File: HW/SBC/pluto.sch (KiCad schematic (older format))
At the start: 0 parts

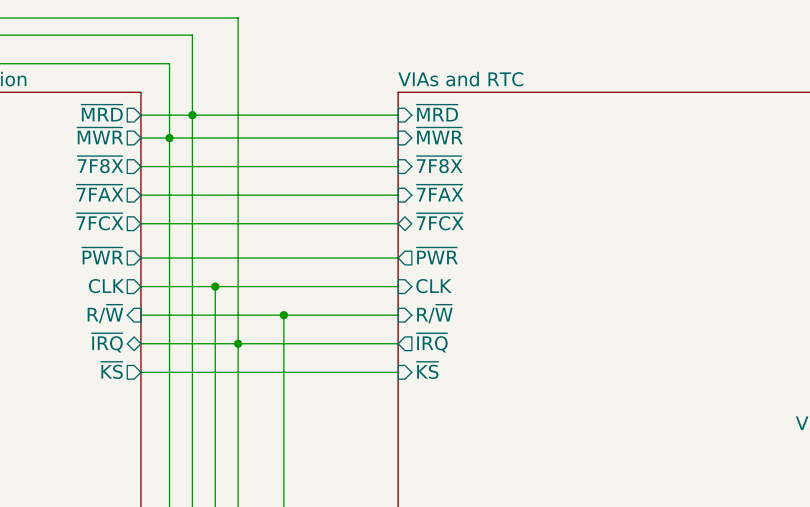
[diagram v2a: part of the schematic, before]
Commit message: Small changes to schematics. Futher development of BIOS.
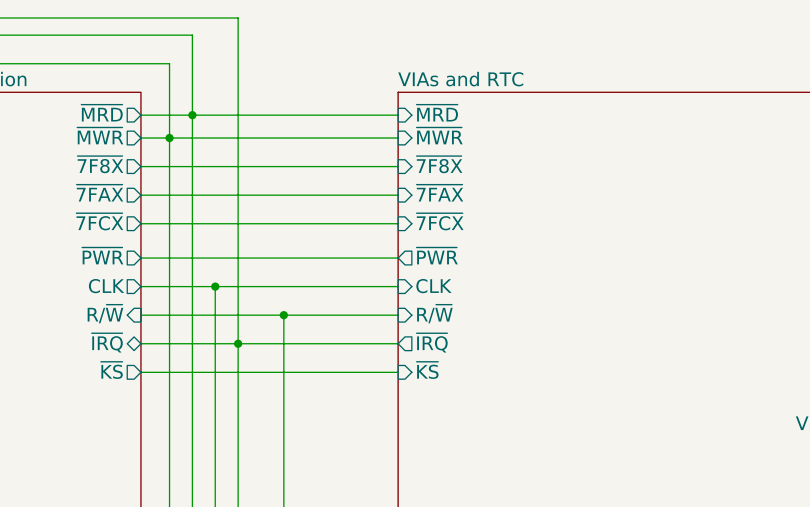
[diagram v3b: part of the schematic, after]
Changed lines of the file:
@@
 LIBS:transistor
 LIBS:uln-ic
-LIBS:IDE_interface
+LIBS:+1.8V
+LIBS:+3.3V
+LIBS:+5V
+LIBS:+9V
+LIBS:25AA02EXXX-XOT
+LIBS:74LVC8T245
+LIBS:4021
+LIBS:7408
+LIBS:74125
+LIBS:74138
+LIBS:74148
+LIBS:74151
+LIBS:74157
+LIBS:74541
+LIBS:ANT
+LIBS:AP6502
+LIBS:AUDIO-JACK-3
+LIBS:AUDIO-JACK-6
+LIBS:BATTERY
+LIBS:BELFUSE-08B0-1X1T-06-F
+LIBS:C
+LIBS:CP
+LIBS:CRYSTAL
+LIBS:CRYSTAL-14
+LIBS:CVAR
+LIBS:DIODE
+LIBS:DIODES-AP3211
+LIBS:DIODESCH
+LIBS:DIODEZENER
+LIBS:DMMT5401
+LIBS:EDISON-BULB-E10
+LIBS:EDISON-SOCKET-E10
+LIBS:ENC28J60
+LIBS:FTDI-PLUG
+LIBS:GNDPWR
+LIBS:~GNDPWR
+LIBS:INDUCTOR
+LIBS:INTEL-EDISON-COMPUTE-MODULE
+LIBS:IS31AP4066D
+LIBS:JTAG
+LIBS:JTAG10
+LIBS:LATTICE-LC4256
+LIBS:LED
+LIBS:LED-BI
+LIBS:LED-BI-COMMON-CATHODE
+LIBS:LM324
+LIBS:LM1875
+LIBS:MAX3221
+LIBS:MC33926
+LIBS:MC34063A
+LIBS:MCP49X1
+LIBS:MCP3204
+LIBS:MECH
+LIBS:MIC2039
+LIBS:MIC2288
+LIBS:MICROSD-AMPHENOL-114-00841-68
+LIBS:MOSFET-N
+LIBS:MOSFET-N-123
+LIBS:MOSFET-N-134
+LIBS:MOSFET-P
+LIBS:NPN
+LIBS:nRF8001
+LIBS:NXPUDA1334ATS
+LIBS:OPAMP-DUAL
+LIBS:P01
+LIBS:P02
+LIBS:P03
+LIBS:P05
+LIBS:P06
+LIBS:P06-MOTOR
+LIBS:P08
+LIBS:P10
+LIBS:P22
+LIBS:P24
+LIBS:PHOTO_TRANSISTOR
+LIBS:PIEZO
+LIBS:PNP
+LIBS:POLYFUSE
+LIBS:POT
+LIBS:PWR_FLAG
+LIBS:QRE1113
+LIBS:R
+LIBS:RASPBERRYPI
+LIBS:RASPBERRYPI2
+LIBS:RBUS8
+LIBS:RN4020
+LIBS:ROBOT-P10-IO
+LIBS:RS-232-DB-9-DTE
+LIBS:SEN-SHT3x-DIS
+LIBS:SERVO
+LIBS:SI4737-C40-GM
+LIBS:SI4737-GU
+LIBS:SKYWORKS-AAT1217-3.3
+LIBS:SPDT
+LIBS:SPST
+LIBS:SPST-4PIN
+LIBS:SST25VF032B-S2A
+LIBS:SST26VF032B
+LIBS:ST-LIS3MDL
+LIBS:STM32-32PIN
+LIBS:STM32-48PIN
+LIBS:STM32-64PIN
+LIBS:STM32SWDUART
+LIBS:ST-SWD
+LIBS:ST-TDA7266
+LIBS:SWD
+LIBS:TCS3472
+LIBS:TI-ADS7866
+LIBS:TICC3000
+LIBS:TIREF30XX
+LIBS:TP
+LIBS:TS5A623157
+LIBS:TSV631
+LIBS:TVS-DIODE
+LIBS:TXB0108-PW
+LIBS:USBAB
+LIBS:Vcc
+LIBS:Vdd
+LIBS:VIN
+LIBS:VREG
+LIBS:VREG_VOUTCENTER
 LIBS:74xgxx
 LIBS:ac-dc
@@
 F2 "V2PA[0..7]" B R 9275 2350 60
 F3 "D[0..7]" B R 9275 1650 60
-F4 "~7FCX" B L 7025 1475 60
+F4 "~7FCX" I L 7025 1475 60
 F5 "A[0..15]" I R 9275 1475 60
 F6 "~PWR" O L 7025 1625 60
